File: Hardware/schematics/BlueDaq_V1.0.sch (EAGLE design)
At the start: 75 parts, among them IC1 MEGA8-AI, Q1 MMBT2222, Q2 MMBT2222, Q3 MMBT2222, Q4 MMBT2222, U1 MCP73831, U2 TPS61200, U3 BME280, U4 MIC5225-3.3, U5 MIC5219 5V, X1 USB-MICROB, X2 3.5mm, X4 3.5mm, Y1 16 mhz

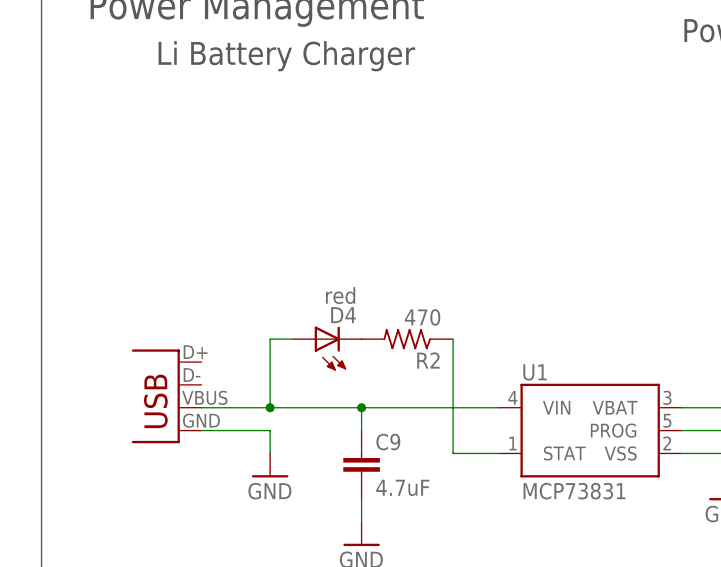
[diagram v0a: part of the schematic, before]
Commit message: fixed comps being too dang small
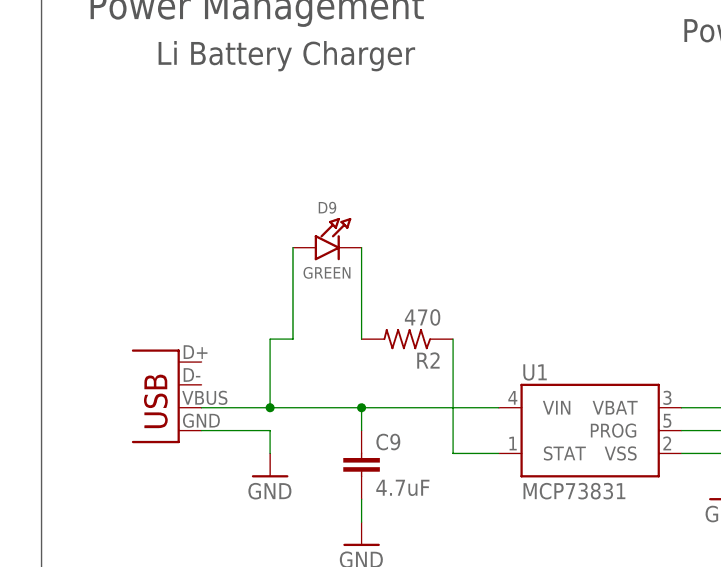
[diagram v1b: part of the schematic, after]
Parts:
- removed D4: red, SparkFun:LED0603
- added D9: GREEN, microbuilder:LED0805_NOOUTLINE
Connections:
- net N$23: now also D9.A; no longer D4.A
- net N$4: now also D9.C; no longer D4.C
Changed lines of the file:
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@@
 <part name="GND18" library="supply1" deviceset="GND" device=""/>
 <part name="GND20" library="supply1" deviceset="GND" device=""/>
-<part name="D4" library="SparkFun" deviceset="LED" device="0603" value="red"/>
 <part name="GND10" library="supply1" deviceset="GND" device=""/>
 <part name="U1" library="SparkFun" deviceset="MCP73831" device=""/>
@@
 <part name="C15" library="microbuilder" deviceset="CAP_CERAMIC" device="0805-NOOUTLINE" value="10uF"/>
 <part name="U$21" library="microbuilder" deviceset="GND" device=""/>
+<part name="D9" library="microbuilder" deviceset="LED" device="0805_NOOUTLINE" value="GREEN"/>
 </parts>
 <sheets>
@@
 <instance part="GND18" gate="1" x="45.72" y="185.42"/>
 <instance part="GND20" gate="1" x="99.06" y="185.42"/>
-<instance part="D4" gate="G$1" x="40.64" y="208.28" rot="R90"/>
 <instance part="GND10" gate="1" x="35.56" y="193.04"/>
 <instance part="U1" gate="G$1" x="71.12" y="198.12"/>
@@
 <instance part="C15" gate="G$1" x="185.42" y="210.82"/>
 <instance part="U$21" gate="G$1" x="185.42" y="205.74"/>
+<instance part="D9" gate="G$1" x="43.18" y="218.44"/>
 </instances>
 <busses>
@@
 <net name="N$4" class="0">
 <segment>
-<pinref part="D4" gate="G$1" pin="C"/>
 <pinref part="R2" gate="G$1" pin="2"/>
+<pinref part="D9" gate="G$1" pin="C"/>
+<wire x1="45.72" y1="218.44" x2="45.72" y2="208.28" width="0.1524" layer="91"/>
 </segment>
 </net>
@@
 <wire x1="45.72" y1="198.12" x2="45.72" y2="200.66" width="0.1524" layer="91"/>
 <wire x1="35.56" y1="200.66" x2="45.72" y2="200.66" width="0.1524" layer="91"/>
-<wire x1="38.1" y1="208.28" x2="35.56" y2="208.28" width="0.1524" layer="91"/>
 <wire x1="35.56" y1="208.28" x2="35.56" y2="200.66" width="0.1524" layer="91"/>
 <wire x1="27.94" y1="200.66" x2="35.56" y2="200.66" width="0.1524" layer="91"/>
 <junction x="35.56" y="200.66"/>
 <pinref part="C9" gate="G$1" pin="1"/>
-<pinref part="D4" gate="G$1" pin="A"/>
 <pinref part="X1" gate="G$1" pin="VBUS"/>
 <pinref part="U1" gate="G$1" pin="VIN"/>
 <wire x1="45.72" y1="200.66" x2="60.96" y2="200.66" width="0.1524" layer="91"/>
 <junction x="45.72" y="200.66"/>
-</segment>
-</net>
+<pinref part="D9" gate="G$1" pin="A"/>
+<wire x1="35.56" y1="208.28" x2="38.1" y2="208.28" width="0.1524" layer="91"/>
+<wire x1="38.1" y1="208.28" x2="38.1" y2="218.44" width="0.1524" layer="91"/>
+</segment>
+</net>
